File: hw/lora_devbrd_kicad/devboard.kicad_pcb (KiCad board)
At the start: 2 copper layers, 32 parts, among them J1 Conn_01x11_Male, J2 Conn_01x11_Male, J3 Conn_01x04_Male, J4 USB_B_Micro, J5 Conn_01x04_Male, J6 Conn_01x04_Male, U1 rhf78-052, U2 LM1117-3.3, U3 FT232RL

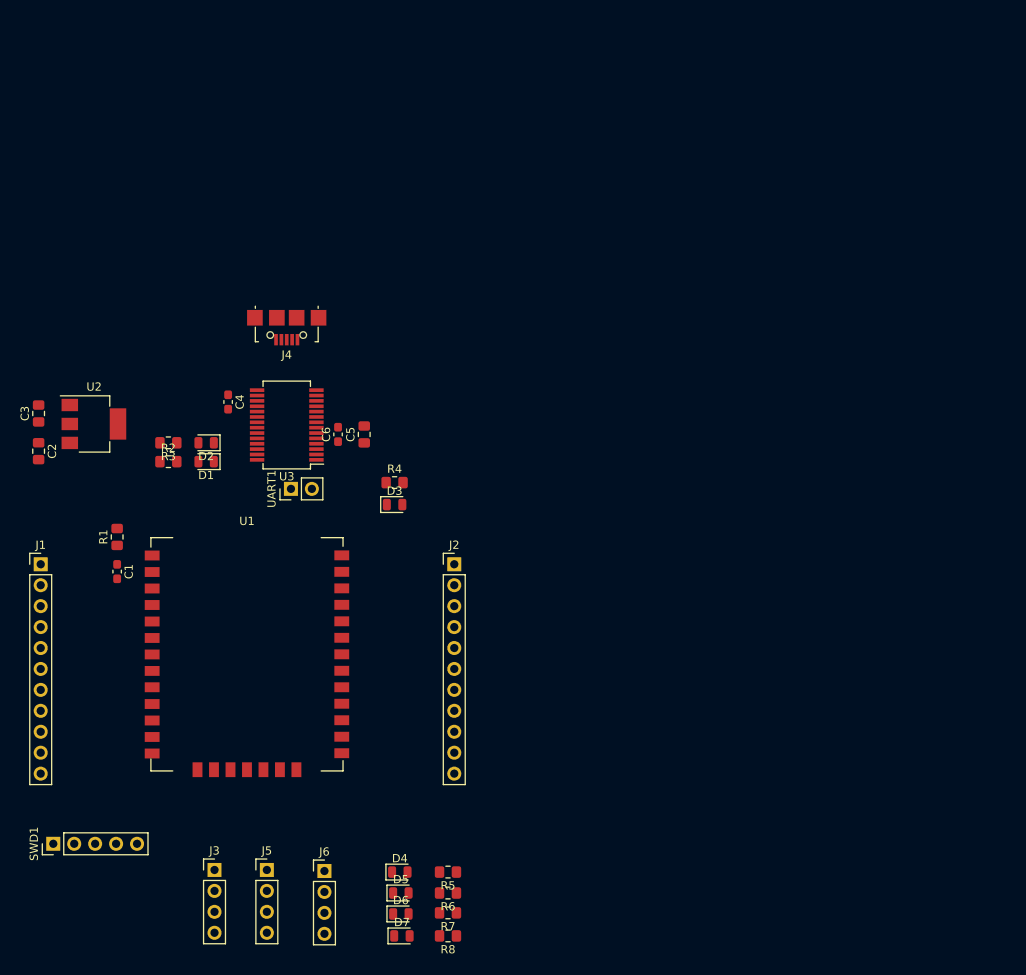
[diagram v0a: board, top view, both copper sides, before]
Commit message: MISC: [kicad] sets top layer componetns to it's places
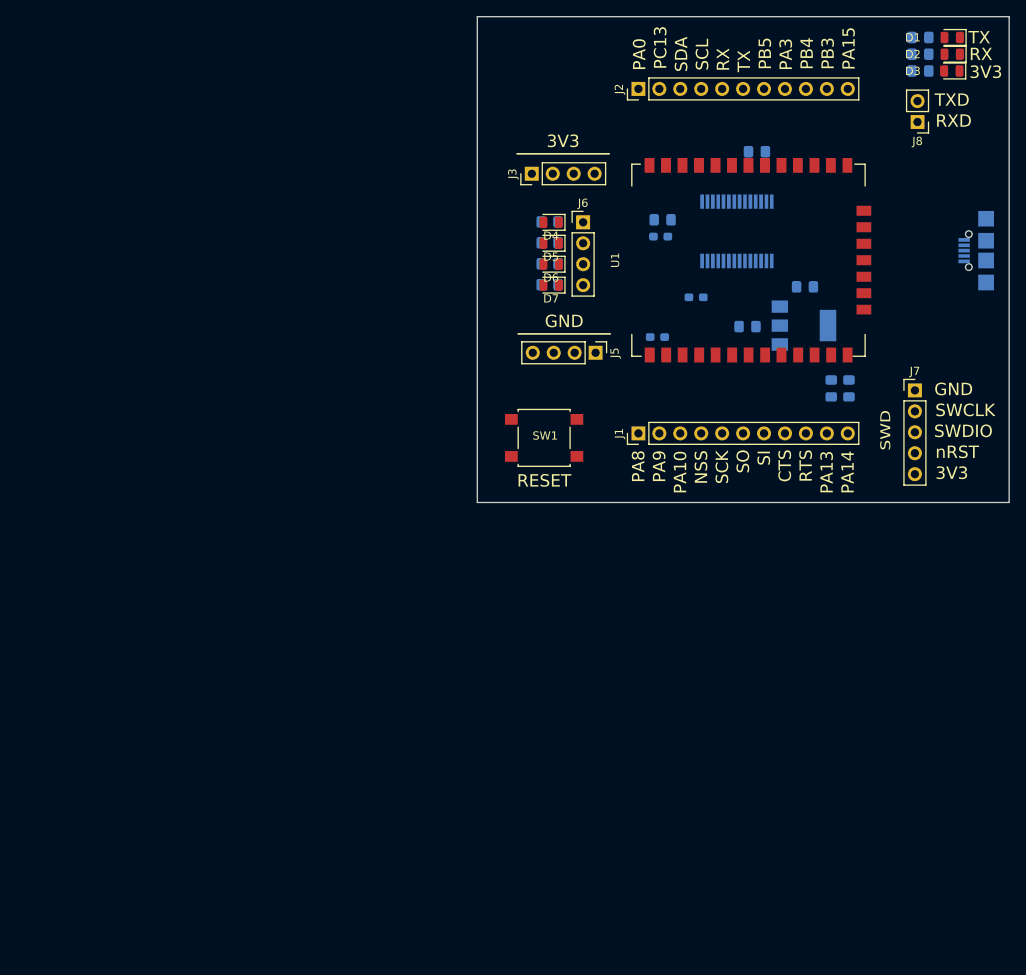
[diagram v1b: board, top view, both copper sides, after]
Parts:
- removed SWD1: Conn_01x05_Male, Connector_PinHeader_2.54mm:PinHeader_1x05_P2.54mm_Vertical
- removed UART1: Conn_01x02_Male, Connector_PinHeader_2.54mm:PinHeader_1x02_P2.54mm_Vertical
- added J7: SWD, Connector_PinHeader_2.54mm:PinHeader_1x05_P2.54mm_Vertical, F.Cu at (168.8, 62.5)
- added J8: Conn_01x02_Male, Connector_PinHeader_2.54mm:PinHeader_1x02_P2.54mm_Vertical, F.Cu at (169.1, 29.9)
- added R10: 440, Resistor_SMD:R_0805_2012Metric_Pad1.15x1.40mm_HandSolder, B.Cu at (160.8, 62.2)
- added R9: 440, Resistor_SMD:R_0805_2012Metric_Pad1.15x1.40mm_HandSolder, B.Cu at (158.6, 62.2)
- added SW1: FSM8JSMATR, Button_Switch_SMD:SW_SPST_B3S-1000, F.Cu at (123.8, 68.2)
- C1, C2, C3, C4, C5, C6, J4, R1, R2, R3, R4, R5, R6, R7, R8, U2, U3: moved to B.Cu
- J3: value Conn_01x04_Male -> 3.3V
- J5: value Conn_01x04_Male -> GND
- J6: value Conn_01x04_Male -> LEDS
- moved R2 104.7 mm to (169.4, 19.7)
- moved D1 104.1 mm to (173.3, 19.7)
- moved R3 102.7 mm to (169.4, 21.7), turned to 0 degrees
- moved D2 102.0 mm to (173.3, 21.7)
- moved C2 95.1 mm to (155.4, 49.9), turned to 0 degrees
- moved J3 92.8 mm to (122.3, 36.2), turned to 90 degrees
- moved R1 90.6 mm to (149.6, 33.5), turned to 180 degrees
- moved U2 87.0 mm to (155.3, 54.6)
- moved C3 86.6 mm to (148.5, 54.7), turned to 180 degrees
- moved D3 85.6 mm to (173.3, 23.7), turned to 180 degrees
- moved J6 84.7 mm to (128.5, 42.1)
- moved J4 84.2 mm to (176.2, 45.5), turned to 270 degrees
- moved R4 81.0 mm to (169.4, 23.7)
- moved D7 81.0 mm to (124.6, 49.7), turned to 180 degrees
- moved D4 80.9 mm to (124.6, 42.1), turned to 180 degrees
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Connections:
- J1 pad 10: SWDIO -> Net-(J1-Pad10)
- J1 pad 11: SWCLK -> Net-(J1-Pad11)
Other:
- board outline added: 64.5 x 58.9 mm
- board text added: "3V3"
- board text added: "CTS"
- board text added: "GND"
- board text added: "NSS"
- board text added: "PA0"
- board text added: "PA10"
- board text added: "PA13"
- board text added: "PA14"
- board text added: "PA15"
- board text added: "PA3"
- board text added: "PA8"
- board text added: "PA9"
- board text added: "PB3"
- board text added: "PB4"
- board text added: "PB5"
- board text added: "PC13"
- board text added: "RESET"
- board text added: "RTS"
- board text added: "RX"
- board text added: "RXD"
- board text added: "SCK"
- board text added: "SCL"
- board text added: "SDA"
- board text added: "SI"
- board text added: "SO"
- board text added: "SWCLK"
- board text added: "SWD"
- board text added: "SWDIO"
- board text added: "TX"
- board text added: "TXD"
- board text added: "nRST"

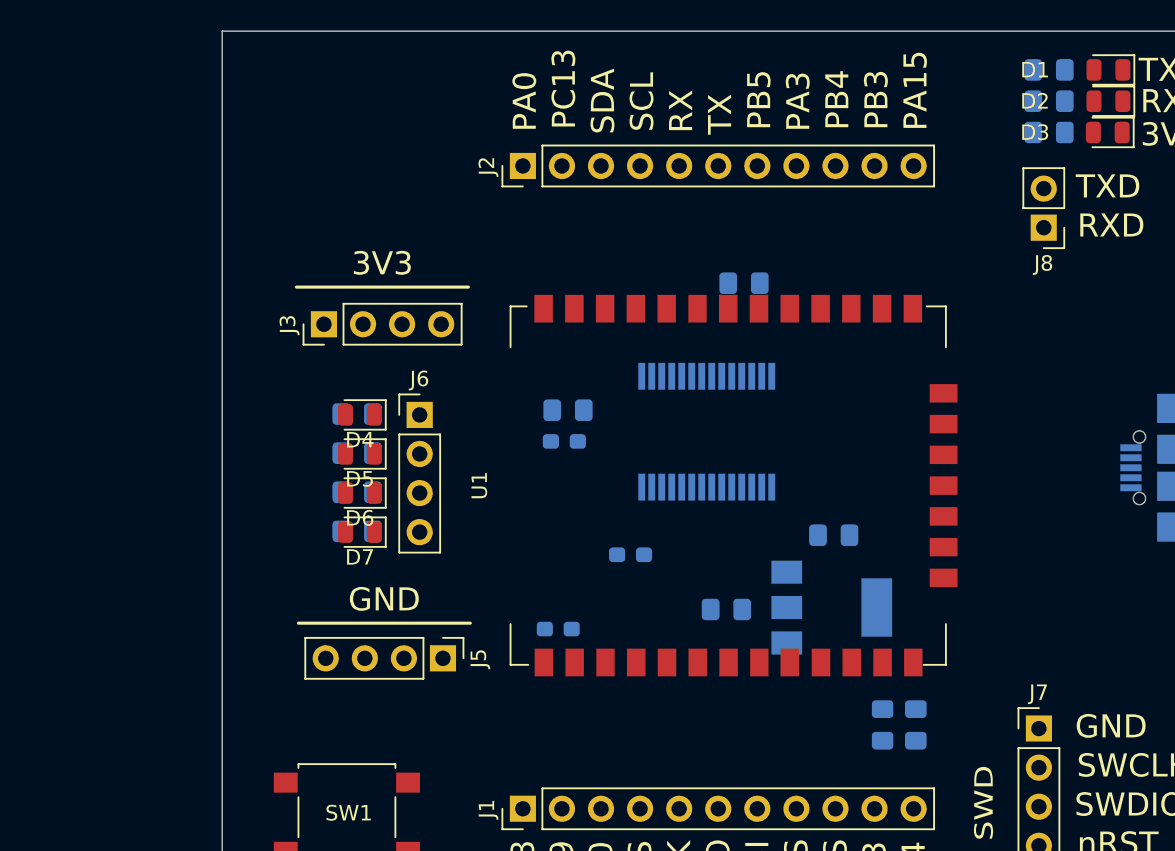
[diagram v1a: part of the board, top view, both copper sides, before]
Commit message: WIP: [kicad] changed footprints for R and C to 1206
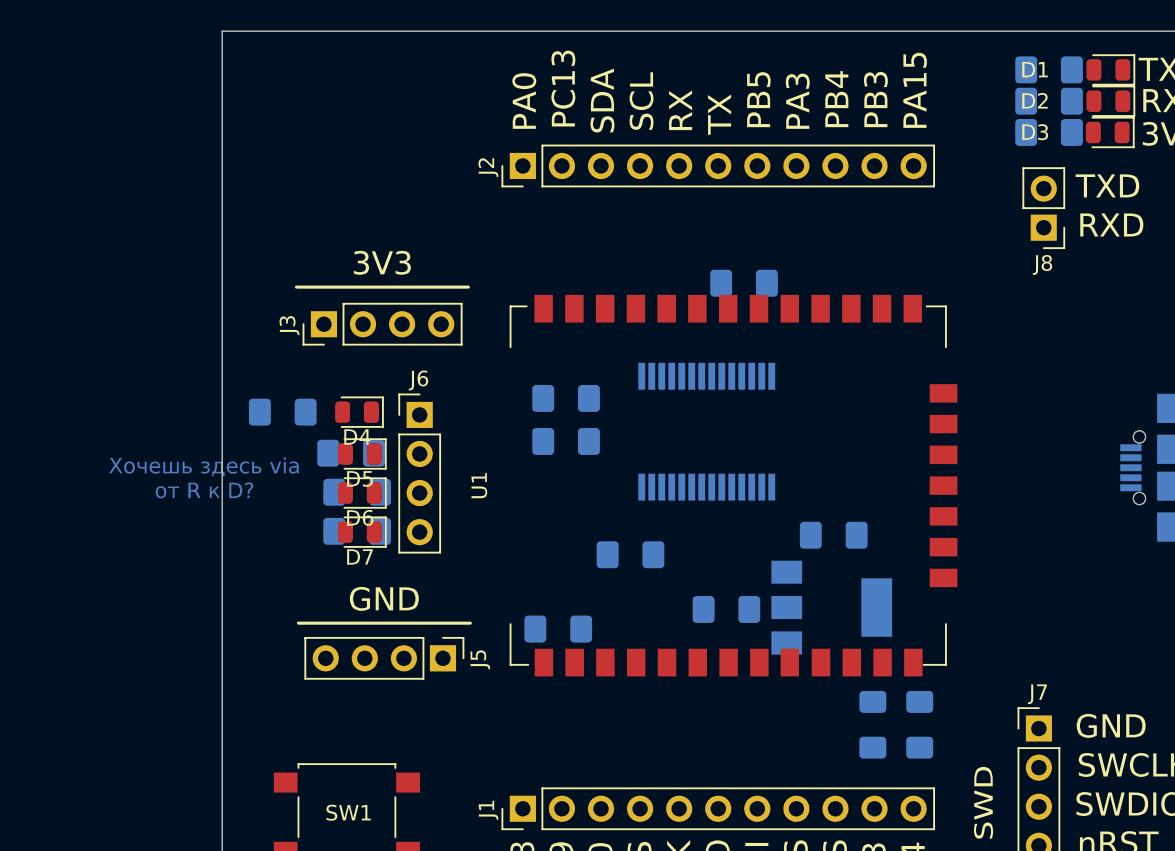
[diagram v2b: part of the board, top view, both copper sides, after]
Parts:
- C1, C4, C6: footprint Capacitor_SMD:C_0603_1608Metric_Pad1.05x0.95mm_HandSolder -> Capacitor_SMD:C_1206_3216Metric_Pad1.42x1.75mm_HandSolder
- C2, C3, C5: footprint Capacitor_SMD:C_0805_2012Metric_Pad1.15x1.40mm_HandSolder -> Capacitor_SMD:C_1206_3216Metric_Pad1.42x1.75mm_HandSolder
- R1, R10, R2, R3, R4, R5, R6, R7, R8, R9: footprint Resistor_SMD:R_0805_2012Metric_Pad1.15x1.40mm_HandSolder -> Resistor_SMD:R_1206_3216Metric_Pad1.42x1.75mm_HandSolder
- moved R5 4.84 mm to (119.6, 41.9), turned to 0 degrees
- moved C5 0.77 mm to (138.0, 41.0)
- moved R9 0.64 mm to (158.0, 62.2)
- moved R6 0.39 mm to (124.1, 44.6)
- moved D4 0.26 mm to (124.5, 41.9)
- moved R10 0.25 mm to (161.0, 62.2)
- moved C6 0.11 mm to (138.0, 43.8)
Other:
- board text added: "Хочешь здесь via от R к D?"

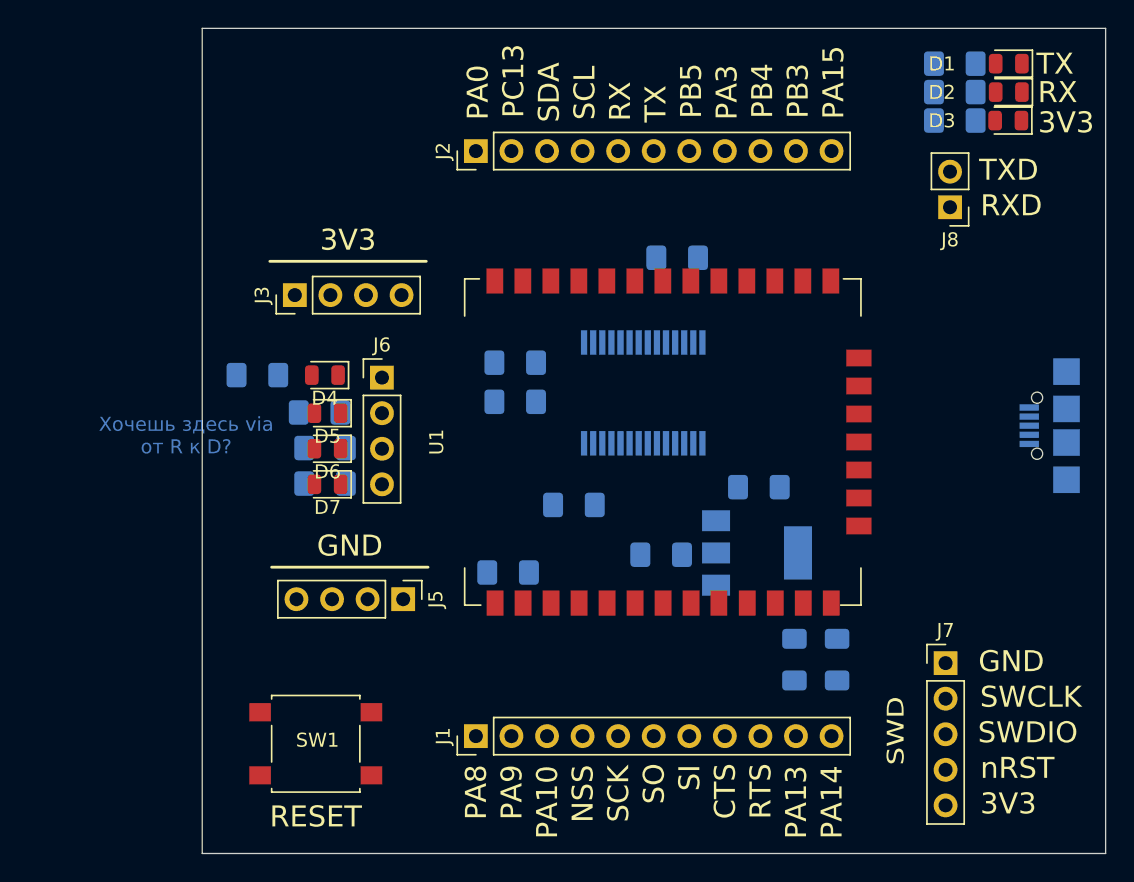
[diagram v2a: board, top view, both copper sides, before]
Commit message: WIP: [kicad] Components and designators are placed finally
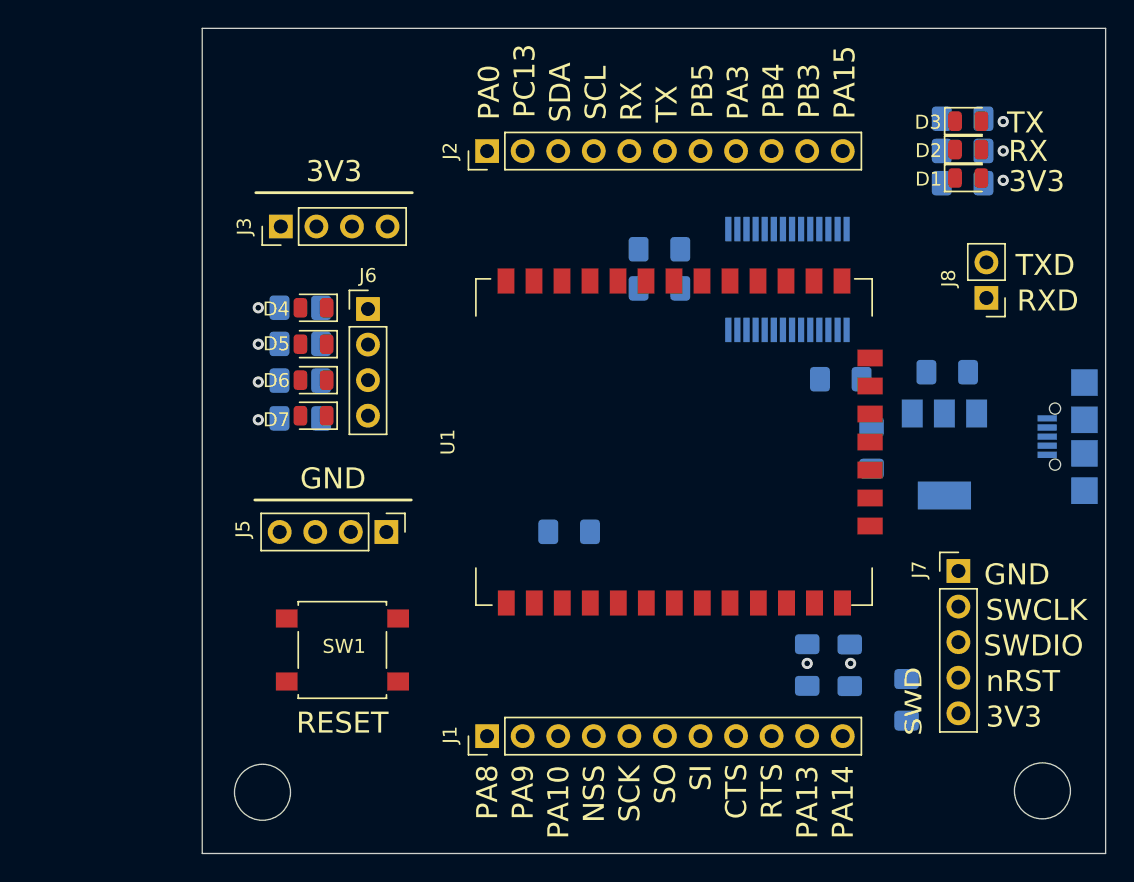
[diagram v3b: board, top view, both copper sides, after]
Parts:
- added REF**: MountingHole_4mm, MountingHole:MountingHole_4mm, F.Cu at (120.0, 71.7)
- added REF**: MountingHole_4mm, MountingHole:MountingHole_4mm, F.Cu at (175.7, 71.6)
- moved R1 35.6 mm to (166.0, 65.1), turned to 90 degrees
- moved C4 21.1 mm to (161.3, 42.2), turned to 0 degrees
- moved C3 16.9 mm to (163.5, 47.1), turned to 90 degrees
- moved C2 15.8 mm to (168.9, 41.7), turned to 180 degrees
- moved U2 15.1 mm to (168.7, 47.6), turned to 270 degrees
- moved C5 13.1 mm to (148.3, 32.9)
- moved U3 13.1 mm to (157.5, 35.1)
- moved C6 13.1 mm to (148.3, 35.7)
- moved D1 8.67 mm to (170.4, 27.8), turned to 0 degrees
- moved R2 8.55 mm to (170.0, 28.2)
- moved J8 6.98 mm to (171.7, 36.4)
- moved SW1 6.96 mm to (125.7, 61.5)
- moved J7 6.64 mm to (169.7, 55.9)
- moved R5 5.70 mm to (122.7, 37.1), turned to 180 degrees
- moved C1 5.24 mm to (141.9, 53.1)
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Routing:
- net SWDIO: vias 0 -> 1
- net SWCLK: vias 0 -> 1
- net Net-(D7-Pad2): vias 0 -> 1
- net Net-(D6-Pad2): vias 0 -> 1
- net Net-(D5-Pad2): vias 0 -> 1
- net Net-(D4-Pad2): vias 0 -> 1
- net Net-(D3-Pad2): vias 0 -> 1
- net Net-(D2-Pad2): vias 0 -> 1
- net Net-(D1-Pad2): vias 0 -> 1
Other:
- board text removed: "Хочешь здесь via от R к D?"

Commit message: WIP: [kicad] Routed; antennas will be added yet
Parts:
- added REF**: MountingHole_4mm, MountingHole:MountingHole_4mm, F.Cu at (175.9, 21.5)
- added REF**: MountingHole_4mm, MountingHole:MountingHole_4mm, F.Cu at (120.0, 21.5)
- moved C4 11.8 mm to (149.5, 41.4), turned to 180 degrees
- moved D3 6.60 mm to (170.2, 30.4)
- moved R4 6.60 mm to (169.8, 30.2)
- moved C1 4.57 mm to (137.7, 54.9)
- moved U3 2.72 mm to (157.5, 37.8), turned to 180 degrees
- moved D1 2.61 mm to (170.2, 25.2)
- moved R2 2.61 mm to (169.8, 25.6)
- moved C5 2.41 mm to (147.2, 35.1), turned to 90 degrees
- moved D2 2.01 mm to (170.2, 27.8)
- moved R3 2.01 mm to (169.8, 27.9)
- moved J8 1.94 mm to (172.8, 34.8), turned to 270 degrees
- moved C6 1.79 mm to (150.0, 35.1), turned to 90 degrees
- moved J7 1.12 mm to (169.2, 56.9)
- moved R1 1.12 mm to (165.5, 66.1)
- moved C2 1.12 mm to (170.0, 41.9)
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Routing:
- net GND: track 0.00 -> 204.4 mm, vias 0 -> 5
- net +3V3: track 0.00 -> 165.7 mm, vias 0 -> 3
- net nRST: track 0.00 -> 94.1 mm
- net D-: track 0.00 -> 37.0 mm
- net D+: track 0.00 -> 37.0 mm
- net PA15: track 0.00 -> 31.3 mm
- net PB3: track 0.00 -> 29.3 mm
- net PB4: track 0.00 -> 27.8 mm
- net TX_LED: track 0.00 -> 22.5 mm, vias 0 -> 1
- net RX_LED: track 0.00 -> 21.6 mm, vias 0 -> 1
- net PA3: track 0.00 -> 18.9 mm
- net PC13: track 0.00 -> 18.3 mm
- net SDA: track 0.00 -> 18.3 mm
- net SCL: track 0.00 -> 17.7 mm
- net SWDIO: track 0.00 -> 17.2 mm
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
